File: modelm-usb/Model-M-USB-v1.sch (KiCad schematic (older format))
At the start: 60 parts, among them J1 Conn_01x16, J2 Conn_01x08, J3 Conn_01x05_Male, J4 USB_B, J5 Conn_01x02_Male, J6 Conn_01x04, J7 Conn_01x05_Male, J8 Conn_01x02, J9 AVR-ISP-6, Q1 2N7002, SW1 SW_Push, U1 ATmega32U4-MU, U2 PRTR5V0U2X, U3 74HC165, U4 MAX809T, U5 74HC165, Y1 16.0MHz, Y2 16.0MHz

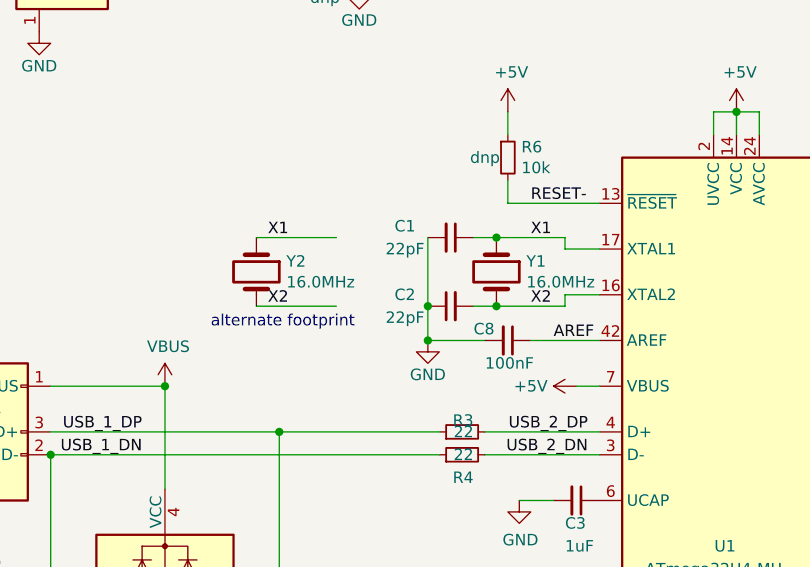
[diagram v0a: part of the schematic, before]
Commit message: change C1, C2 after fine-tuning crystal frequency
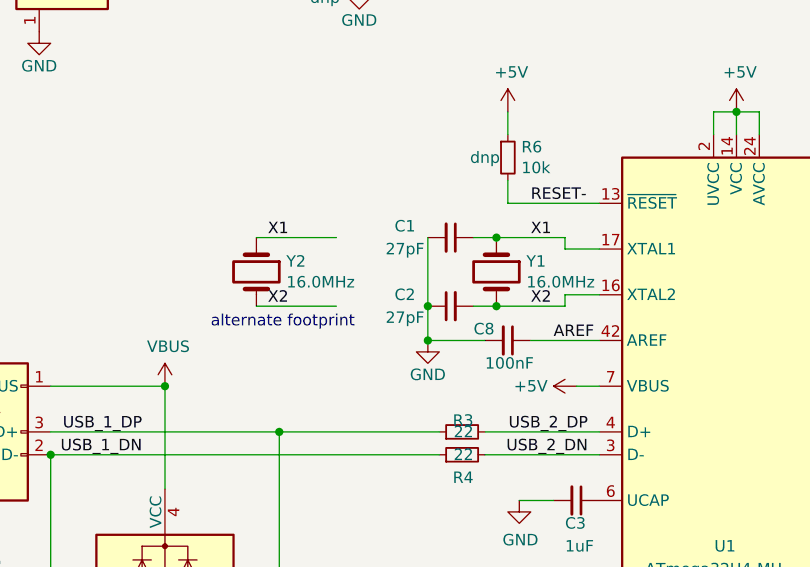
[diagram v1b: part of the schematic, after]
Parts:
- C1, C2: value 22pF -> 27pF
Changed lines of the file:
@@
 P 3100 2550
 F 0 "C1" V 3050 2350 50  0000 C CNN
-F 1 "22pF" V 3150 2350 50  0000 C CNN
+F 1 "27pF" V 3150 2350 50  0000 C CNN
 F 2 "Capacitor_SMD:C_0603_1608Metric_Pad1.05x0.95mm_HandSolder" H 3100 2550 50  0001 C CNN
 F 3 "~" H 3100 2550 50  0001 C CNN
@@
 P 3100 2850
 F 0 "C2" V 3150 3050 50  0000 C CNN
-F 1 "22pF" V 3050 3050 50  0000 C CNN
+F 1 "27pF" V 3050 3050 50  0000 C CNN
 F 2 "Capacitor_SMD:C_0603_1608Metric_Pad1.05x0.95mm_HandSolder" H 3100 2850 50  0001 C CNN
 F 3 "~" H 3100 2850 50  0001 C CNN
